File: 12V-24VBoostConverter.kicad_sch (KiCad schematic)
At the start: 16 parts, among them IC2 TPS613771RYHR

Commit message: small rev3 changes
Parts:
- added C22, C23: 22u, symbol Device:C
- C12: value 56u -> 22u
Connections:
- net GND: now also C22.2, C23.2
- net at C12.1, C41.1, F3.1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: now also C22.1, C23.1
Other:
- note removed: "change 56uF into 22u"
- moved on the sheet: C41

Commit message: revA4
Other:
- moved on the sheet: C10, C11, C12, C22, C23, C41, C7, C8, C9, F3, IC2, L2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

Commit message: RevA5
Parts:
- added D6: D_Schottky, SK34A-LTP, symbol Device:D_Schottky
- C10, C11, C9: footprint (none) -> Capacitor_SMD:C_0603_1608Metric
- C12, C22, C23, C41, C7, C8: footprint (none) -> Capacitor_SMD:C_0805_2012Metric
- F3: footprint (none) -> Fuse:Fuse_0805_2012Metric
- L2: footprint (none) -> Inductor_SMD:L_0603_1608Metric
- R10, R11, R12, R7: footprint (none) -> Resistor_SMD:R_0603_1608Metric
- R8: value 884.946 -> 1k; footprint (none) -> Resistor_SMD:R_0603_1608Metric
- R9: value 15k -> 29.4k; footprint (none) -> Resistor_SMD:R_0603_1608Metric
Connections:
- net at C12.1, C22.1, C23.1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: now also D6.2 (A); no longer F3.1
- new net: D6.1 (K), F3.1
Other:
- note added: "Ipeak = 0.54 * 160k/29.4k (standard component) Ipeak = 2.938 A"
- note added: "find new diode w low voltage drop"
- note removed: "Ipeak = I(avg input) + I(L)/2 = 5+ 0.75 = 5.75 --> 6A I(L) = 0.3 * 5 = 1.5 Ipeak = 6A 6 = 0.54 * 160k/Rlim Rlim = 14.4k or Ipeak = 0.54 * 160k/15k (standard component) Ipeak = 5.76A"
- moved on the sheet: F3
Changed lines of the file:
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@@
 		)
 	)
-	(text "Ipeak = I(avg input) + I(L)/2 = 5+ 0.75 = 5.75 --> 6A\nI(L) = 0.3 * 5 = 1.5\nIpeak = 6A\n6 = 0.54 * 160k/Rlim\nRlim = 14.4k\n\nor\n\nIpeak = 0.54 * 160k/15k (standard component)\nIpeak = 5.76A"
+	(text "Ipeak = 0.54 * 160k/29.4k (standard component)\nIpeak = 2.938 A"
 		(exclude_from_sim no)
-		(at 101.6 117.094 0)
+		(at 101.854 109.728 0)
 		(effects
 			(font
@@
 		)
 	)
+	(text "find new diode w low voltage drop"
+		(exclude_from_sim no)
+		(at 127.254 27.178 0)
+		(effects
+			(font
+				(size 1.27 1.27)
+			)
+			(justify left)
+		)
+	)
 	(junction
 		(at 86.36 29.21)
@@
 	(wire
 		(pts
+			(xy 128.27 43.18) (xy 132.08 43.18)
+		)
+		(stroke
+			(width 0)
+			(type default)
+		)
+	)
+	(wire
+		(pts
 			(xy 54.61 52.07) (xy 54.61 54.61)
 		)
@@
 	(wire
 		(pts
+			(xy 152.4 43.18) (xy 162.56 43.18)
+		)
+		(stroke
+			(width 0)
+			(type default)
+		)
+	)
+	(wire
+		(pts
 			(xy 128.27 49.53) (xy 128.27 52.07)
 		)
@@
 	(wire
 		(pts
-			(xy 149.86 43.18) (xy 162.56 43.18)
-		)
-		(stroke
-			(width 0)
-			(type default)
-		)
-	)
-	(wire
-		(pts
 			(xy 93.98 29.21) (xy 95.25 29.21)
 		)
@@
 	(wire
 		(pts
-			(xy 128.27 43.18) (xy 142.24 43.18)
-		)
-		(stroke
-			(width 0)
-			(type default)
-		)
-	)
-	(wire
-		(pts
 			(xy 138.43 59.69) (xy 138.43 62.23)
 		)
@@
 	(wire
 		(pts
+			(xy 139.7 43.18) (xy 144.78 43.18)
+		)
+		(stroke
+			(width 0)
+			(type default)
+		)
+	)
+	(wire
+		(pts
 			(xy 87.63 66.04) (xy 87.63 69.85)
 		)
@@
 		(dnp no)
 		(property "Reference" "C10"
-			(at 99.314 80.518 0)
+			(at 100.076 80.264 0)
 			(effects
 				(font
@@
 			)
 		)
-		(property "Footprint" ""
+		(property "Footprint" "Capacitor_SMD:C_0603_1608Metric"
 			(at 96.8248 78.74 0)
 			(effects
@@
 			)
 		)
-		(property "Footprint" ""
+		(property "Footprint" "Capacitor_SMD:C_0805_2012Metric"
 			(at 86.6648 69.85 0)
 			(effects
@@
 			)
 		)
-		(property "Footprint" ""
+		(property "Footprint" "Capacitor_SMD:C_0603_1608Metric"
 			(at 91.7448 69.85 0)
 			(effects
@@
 			)
 		)
-		(property "Value" "884.946"
+		(property "Value" "1k"
 			(at 55.88 49.784 0)
 			(effects
@@
 			)
 		)
-		(property "Footprint" ""
+		(property "Footprint" "Resistor_SMD:R_0603_1608Metric"
 			(at 52.832 48.26 90)
 			(effects
@@
 			)
 		)
-		(property "Footprint" ""
+		(property "Footprint" "Resistor_SMD:R_0603_1608Metric"
 			(at 52.832 38.1 90)
 			(effects
@@
 			)
 		)
-		(property "Footprint" ""
+		(property "Footprint" "Resistor_SMD:R_0603_1608Metric"
 			(at 117.602 50.8 90)
 			(effects
@@
 			)
 		)
-		(property "Footprint" ""
+		(property "Footprint" "Inductor_SMD:L_0603_1608Metric"
 			(at 90.17 29.21 0)
 			(effects
@@
 			)
 		)
-		(property "Footprint" ""
+		(property "Footprint" "Capacitor_SMD:C_0805_2012Metric"
 			(at 68.2752 38.1 0)
 			(effects
@@
 			)
 		)
-		(property "Footprint" ""
+		(property "Footprint" "Resistor_SMD:R_0603_1608Metric"
 			(at 117.602 67.31 90)
 			(effects
@@
 			)
 		)
-		(property "Footprint" ""
+		(property "Footprint" "Capacitor_SMD:C_0603_1608Metric"
 			(at 104.14 28.2448 0)
 			(effects
@@
 			)
 		)
-		(property "Footprint" ""
+		(property "Footprint" "Resistor_SMD:R_0603_1608Metric"
 			(at 96.012 73.66 90)
 			(effects
@@
 			)
 		)
-		(property "Value" "15k"
+		(property "Value" "29.4k"
 			(at 68.834 58.42 0)
 			(effects
@@
 			)
 		)
-		(property "Footprint" ""
+		(property "Footprint" "Resistor_SMD:R_0603_1608Metric"
 			(at 65.532 57.15 90)
 			(effects
@@
 	)
 	(symbol
+		(lib_id "Device:D_Schottky")
+		(at 135.89 43.18 0)
+		(mirror y)
+		(unit 1)
+		(exclude_from_sim no)
+		(in_bom yes)
+		(on_board yes)
+		(dnp no)
+		(property "Reference" "D6"
+			(at 136.2075 36.83 0)
+			(effects
+				(font
+					(size 1.27 1.27)
+				)
+			)
+		)
+		(property "Value" "D_Schottky"
+			(at 136.2075 39.37 0)
+			(effects
+				(font
+					(size 1.27 1.27)
+				)
+			)
+		)
+		(property "Footprint" "SK34A-LTP"
+			(at 135.89 43.18 0)
+			(effects
+				(font
+					(size 1.27 1.27)
+				)
+				(hide yes)
+			)
+		)
+		(property "Datasheet" "https://www.mouser.com/datasheet/3/225/1/SK32A-L-SK310A-L(SMA).pdf"
+			(at 135.89 43.18 0)
+			(effects
+				(font
+					(size 1.27 1.27)
+				)
+				(hide yes)
+			)
+		)
+		(property "Description" "Schottky diode"
+			(at 135.89 43.18 0)
+			(effects
+				(font
+					(size 1.27 1.27)
+				)
+				(hide yes)
+			)
+		)
+		(pin "1"
+		)
+		(pin "2"
+		)
+		(instances
+			(project ""
+				(path "/d45494af-ff47-4110-bed2-dd613b557244/a5946dd4-2cac-491d-9b85-f213ab9011e7"
+					(reference "D6")
+					(unit 1)
+				)
+			)
+		)
+	)
+	(symbol
 		(lib_id "Device:C")
 		(at 138.43 55.88 0)
@@
 			)
 		)
-		(property "Footprint" ""
+		(property "Footprint" "Capacitor_SMD:C_0805_2012Metric"
 			(at 139.3952 59.69 0)
 			(effects
@@
 	(symbol
 		(lib_id "Device:Fuse")
-		(at 146.05 43.18 90)
+		(at 148.59 43.18 90)
 		(unit 1)
 		(exclude_from_sim no)
@@
 		(dnp no)
 		(property "Reference" "F3"
-			(at 147.066 41.148 90)
+			(at 149.606 41.148 90)
 			(effects
 				(font
@@
 		)
 		(property "Value" "5"
-			(at 146.558 45.466 90)
+			(at 149.098 45.466 90)
 			(effects
 				(font
@@
 			)
 		)
-		(property "Footprint" ""
-			(at 146.05 44.958 90)
+		(property "Footprint" "Fuse:Fuse_0805_2012Metric"
+			(at 148.59 44.958 90)
 			(effects
 				(font
@@
 		)
 		(property "Datasheet" "~"
-			(at 146.05 43.18 0)
+			(at 148.59 43.18 0)
 			(effects
 				(font
@@
 		)
 		(property "Description" "Fuse"
-			(at 146.05 43.18 0)
+			(at 148.59 43.18 0)
 			(effects
 				(font
@@
 			)
 		)
-		(property "Footprint" ""
+		(property "Footprint" "Capacitor_SMD:C_0805_2012Metric"
 			(at 129.2352 59.69 0)
 			(effects
@@
 			)
 		)
-		(property "Footprint" ""
+		(property "Footprint" "Capacitor_SMD:C_0805_2012Metric"
 			(at 149.5552 59.69 0)
 			(effects
@@
 			)
 		)
-		(property "Footprint" ""
+		(property "Footprint" "Capacitor_SMD:C_0805_2012Metric"
 			(at 159.7152 59.69 0)
 			(effects

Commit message: RevA5 small changes
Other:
- note removed: "find new diode w low voltage drop"
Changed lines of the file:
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@@
-		)
-	)
-	(text "find new diode w low voltage drop"
-		(exclude_from_sim no)
-		(at 127.254 27.178 0)
-		(effects
-			(font
-				(size 1.27 1.27)
-			)
-			(justify left)
 		)
 	)

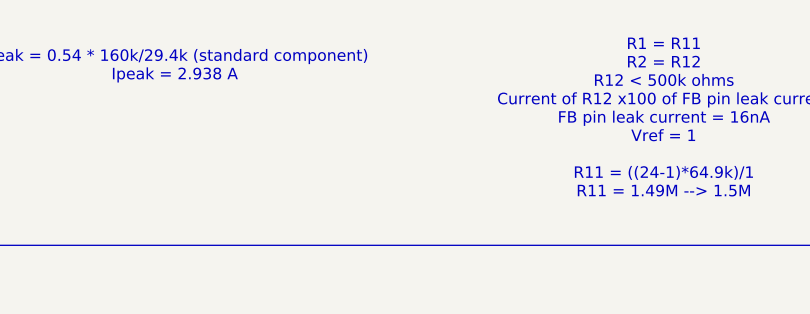
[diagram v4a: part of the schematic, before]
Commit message: RevA6 footprint updates
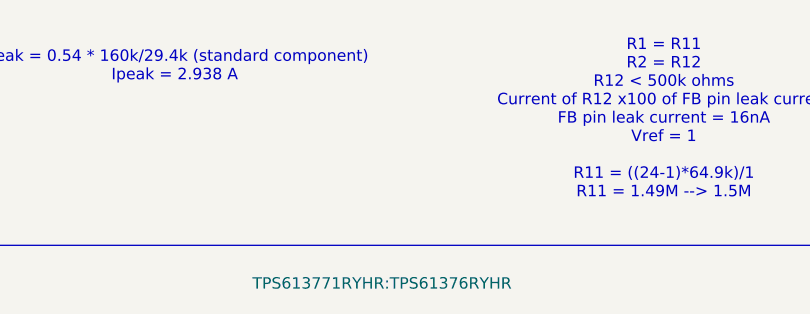
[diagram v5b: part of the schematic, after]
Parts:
- D6: footprint SK34A-LTP -> SK32A_LTP:SDO_DO-214AC-SMA_MCE
- IC2: footprint TPS61376RYHR -> TPS613771RYHR:TPS61376RYHR
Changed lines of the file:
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@@
 			)
 		)
-		(property "Footprint" "TPS61376RYHR"
+		(property "Footprint" "TPS613771RYHR:TPS61376RYHR"
 			(at 110.49 133.02 0)
 			(effects
@@
 				)
 				(justify left top)
-				(hide yes)
 			)
 		)
@@
 			)
 		)
-		(property "Footprint" "SK34A-LTP"
+		(property "Footprint" "SK32A_LTP:SDO_DO-214AC-SMA_MCE"
 			(at 135.89 43.18 0)
 			(effects

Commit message: RevA7 layout
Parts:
- IC2: footprint TPS613771RYHR:TPS61376RYHR -> TPS613771RYHR:VQFN-HR13_RYH_TEX
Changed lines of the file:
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@@
 			)
 		)
-		(property "Footprint" "TPS613771RYHR:TPS61376RYHR"
+		(property "Footprint" "TPS613771RYHR:VQFN-HR13_RYH_TEX"
 			(at 110.49 133.02 0)
 			(effects

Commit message: RevA9 for review
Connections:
- net 24VOut_B4Diodes: now reaches C12.1, C22.1, C23.1, C41.1, D6.2 (A), IC2.4 (VSENSE_1), IC2.5 (VOUT), R11.1

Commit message: RevA9 small changes
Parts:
- renumbered C7 to C1, C8 to C2, C9 to C3, C10 to C4, C11 to C5, C12 to C6, C41 to C7, C22 to C8, C23 to C9, D6 to D1, F3 to F1, IC2 to IC1, L2 to L1, R11 to R10, R12 to R11, R7 to R6, R8 to R7, R9 to R8, R10 to R9
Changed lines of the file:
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@@
 		(on_board yes)
 		(dnp no)
-		(property "Reference" "C10"
+		(property "Reference" "C4"
 			(at 100.076 80.264 0)
 			(effects
@@
 			(project "PS-ChargerInterfacePCB"
 				(path "/d45494af-ff47-4110-bed2-dd613b557244/a5946dd4-2cac-491d-9b85-f213ab9011e7"
-					(reference "C10")
+					(reference "C4")
 					(unit 1)
 				)
@@
 		(dnp no)
 		(fields_autoplaced yes)
-		(property "Reference" "#PWR038"
+		(property "Reference" "#PWR022"
 			(at 68.58 54.61 0)
 			(effects
@@
 			(project "PS-ChargerInterfacePCB"
 				(path "/d45494af-ff47-4110-bed2-dd613b557244/a5946dd4-2cac-491d-9b85-f213ab9011e7"
-					(reference "#PWR038")
+					(reference "#PWR022")
 					(unit 1)
 				)
@@
 		(on_board yes)
 		(dnp no)
-		(property "Reference" "C8"
+		(property "Reference" "C2"
 			(at 85.598 71.374 0)
 			(effects
@@
 			(project "PS-ChargerInterfacePCB"
 				(path "/d45494af-ff47-4110-bed2-dd613b557244/a5946dd4-2cac-491d-9b85-f213ab9011e7"
-					(reference "C8")
+					(reference "C2")
 					(unit 1)
 				)
@@
 		(on_board yes)
 		(dnp no)
-		(property "Reference" "C9"
+		(property "Reference" "C3"
 			(at 94.234 71.374 0)
 			(effects
@@
 			(project "PS-ChargerInterfacePCB"
 				(path "/d45494af-ff47-4110-bed2-dd613b557244/a5946dd4-2cac-491d-9b85-f213ab9011e7"
-					(reference "C9")
+					(reference "C3")
 					(unit 1)
 				)
@@
 		(dnp no)
 		(fields_autoplaced yes)
-		(property "Reference" "#PWR010"
+		(property "Reference" "#PWR020"
 			(at 67.31 45.72 0)
 			(effects
@@
 			(project "PS-ChargerInterfacePCB"
 				(path "/d45494af-ff47-4110-bed2-dd613b557244/a5946dd4-2cac-491d-9b85-f213ab9011e7"
-					(reference "#PWR010")
+					(reference "#PWR020")
 					(unit 1)
 				)
@@
 		(on_board yes)
 		(dnp no)
-		(property "Reference" "R8"
+		(property "Reference" "R7"
 			(at 55.88 47.244 0)
 			(effects
@@
 			(project "PS-ChargerInterfacePCB"
 				(path "/d45494af-ff47-4110-bed2-dd613b557244/a5946dd4-2cac-491d-9b85-f213ab9011e7"
-					(reference "R8")
+					(reference "R7")
 					(unit 1)
 				)
@@
 		(on_board yes)
 		(dnp no)
-		(property "Reference" "R7"
+		(property "Reference" "R6"
 			(at 56.134 36.576 0)
 			(effects
@@
 			(project "PS-ChargerInterfacePCB"
 				(path "/d45494af-ff47-4110-bed2-dd613b557244/a5946dd4-2cac-491d-9b85-f213ab9011e7"
-					(reference "R7")
+					(reference "R6")
 					(unit 1)
 				)
@@
 		(on_board yes)
 		(dnp no)
-		(property "Reference" "#PWR012"
+		(property "Reference" "#PWR023"
 			(at 100.33 73.66 0)
 			(effects
@@
 			(project "PS-ChargerInterfacePCB"
 				(path "/d45494af-ff47-4110-bed2-dd613b557244/a5946dd4-2cac-491d-9b85-f213ab9011e7"
-					(reference "#PWR012")
+					(reference "#PWR023")
 					(unit 1)
 				)
@@
 		(on_board yes)
 		(dnp no)
-		(property "Reference" "R11"
+		(property "Reference" "R10"
 			(at 120.904 49.53 0)
 			(effects
@@
 			(project "PS-ChargerInterfacePCB"
 				(path "/d45494af-ff47-4110-bed2-dd613b557244/a5946dd4-2cac-491d-9b85-f213ab9011e7"
-					(reference "R11")
+					(reference "R10")
 					(unit 1)
 				)
@@
 		(on_board yes)
 		(dnp no)
-		(property "Reference" "L2"
+		(property "Reference" "L1"
 			(at 90.17 27.432 90)
 			(effects
@@
 			(project "PS-ChargerInterfacePCB"
 				(path "/d45494af-ff47-4110-bed2-dd613b557244/a5946dd4-2cac-491d-9b85-f213ab9011e7"
-					(reference "L2")
+					(reference "L1")
 					(unit 1)
 				)
@@
 		(on_board yes)
 		(dnp no)
-		(property "Reference" "C7"
+		(property "Reference" "C1"
 			(at 67.564 32.258 0)
 			(effects
@@
 			(project "PS-ChargerInterfacePCB"
 				(path "/d45494af-ff47-4110-bed2-dd613b557244/a5946dd4-2cac-491d-9b85-f213ab9011e7"
-					(reference "C7")
+					(reference "C1")
 					(unit 1)
 				)
@@
 		(on_board yes)
 		(dnp no)
-		(property "Reference" "IC2"
+		(property "Reference" "IC1"
 			(at 118.11 36.7598 0)
 			(effects
@@
 			(project "PS-ChargerInterfacePCB"
 				(path "/d45494af-ff47-4110-bed2-dd613b557244/a5946dd4-2cac-491d-9b85-f213ab9011e7"
-					(reference "IC2")
+					(reference "IC1")
 					(unit 1)
 				)
@@
 		(on_board yes)
 		(dnp no)
-		(property "Reference" "R12"
+		(property "Reference" "R11"
 			(at 120.65 66.04 0)
 			(effects
@@
 			(project "PS-ChargerInterfacePCB"
 				(path "/d45494af-ff47-4110-bed2-dd613b557244/a5946dd4-2cac-491d-9b85-f213ab9011e7"
-					(reference "R12")
+					(reference "R11")
 					(unit 1)
 				)
@@
 		(dnp no)
 		(fields_autoplaced yes)
-		(property "Reference" "#PWR011"
+		(property "Reference" "#PWR021"
 			(at 67.31 68.58 0)
 			(effects
@@
 			(project "PS-ChargerInterfacePCB"
 				(path "/d45494af-ff47-4110-bed2-dd613b557244/a5946dd4-2cac-491d-9b85-f213ab9011e7"
-					(reference "#PWR011")
+					(reference "#PWR021")
 					(unit 1)
 				)
@@
 		(on_board yes)
 		(dnp no)
-		(property "Reference" "C11"
+		(property "Reference" "C5"
 			(at 97.536 28.194 90)
 			(effects
@@
 			(project "PS-ChargerInterfacePCB"
 				(path "/d45494af-ff47-4110-bed2-dd613b557244/a5946dd4-2cac-491d-9b85-f213ab9011e7"
-					(reference "C11")
+					(reference "C5")
 					(unit 1)
 				)
@@
 		(on_board yes)
 		(dnp no)
-		(property "Reference" "R10"
+		(property "Reference" "R9"
 			(at 99.568 72.39 0)
 			(effects
@@
 			(project "PS-ChargerInterfacePCB"
 				(path "/d45494af-ff47-4110-bed2-dd613b557244/a5946dd4-2cac-491d-9b85-f213ab9011e7"
-					(reference "R10")
+					(reference "R9")
 					(unit 1)
 				)
@@
 		(on_board yes)
 		(dnp no)
-		(property "Reference" "R9"
+		(property "Reference" "R8"
 			(at 68.834 55.88 0)
 			(effects
@@
 			(project "PS-ChargerInterfacePCB"
 				(path "/d45494af-ff47-4110-bed2-dd613b557244/a5946dd4-2cac-491d-9b85-f213ab9011e7"
-					(reference "R9")
+					(reference "R8")
 					(unit 1)
 				)
@@
 		(on_board yes)
 		(dnp no)
-		(property "Reference" "D6"
+		(property "Reference" "D1"
 			(at 136.2075 36.83 0)
 			(effects
@@
 			(project ""
 				(path "/d45494af-ff47-4110-bed2-dd613b557244/a5946dd4-2cac-491d-9b85-f213ab9011e7"
-					(reference "D6")
+					(reference "D1")
 					(unit 1)
 				)
@@
 		(on_board yes)
 		(dnp no)
-		(property "Reference" "C41"
+		(property "Reference" "C7"
 			(at 140.97 54.61 0)
 			(effects
@@
 			(project "PS-ChargerInterfacePCB"
 				(path "/d45494af-ff47-4110-bed2-dd613b557244/a5946dd4-2cac-491d-9b85-f213ab9011e7"
-					(reference "C41")
+					(reference "C7")
 					(unit 1)
 				)
@@
 		(on_board yes)
 		(dnp no)
-		(property "Reference" "F3"
+		(property "Reference" "F1"
 			(at 149.606 41.148 90)
 			(effects
@@
 			(project "PS-ChargerInterfacePCB"
 				(path "/d45494af-ff47-4110-bed2-dd613b557244/a5946dd4-2cac-491d-9b85-f213ab9011e7"
-					(reference "F3")
+					(reference "F1")
 					(unit 1)
 				)
@@
 		(dnp no)
 		(fields_autoplaced yes)
-		(property "Reference" "#PWR013"
+		(property "Reference" "#PWR024"
 			(at 104.14 95.25 0)
 			(effects
@@
 			(project "PS-ChargerInterfacePCB"
 				(path "/d45494af-ff47-4110-bed2-dd613b557244/a5946dd4-2cac-491d-9b85-f213ab9011e7"
-					(reference "#PWR013")
+					(reference "#PWR024")
 					(unit 1)
 				)
@@
 		(on_board yes)
 		(dnp no)
-		(property "Reference" "C12"
+		(property "Reference" "C6"
 			(at 130.81 54.61 0)
 			(effects
@@
 			(project "PS-ChargerInterfacePCB"
 				(path "/d45494af-ff47-4110-bed2-dd613b557244/a5946dd4-2cac-491d-9b85-f213ab9011e7"
-					(reference "C12")
+					(reference "C6")
 					(unit 1)
 				)
@@
 		(on_board yes)
 		(dnp no)
-		(property "Reference" "C22"
+		(property "Reference" "C8"
 			(at 151.13 54.61 0)
 			(effects
@@
 			(project "PS-ChargerInterfacePCB"
 				(path "/d45494af-ff47-4110-bed2-dd613b557244/a5946dd4-2cac-491d-9b85-f213ab9011e7"
-					(reference "C22")
+					(reference "C8")
 					(unit 1)
 				)
@@
 		(dnp no)
 		(fields_autoplaced yes)
-		(property "Reference" "#PWR014"
+		(property "Reference" "#PWR025"
 			(at 134.62 69.85 0)
 			(effects
@@
 			(project "PS-ChargerInterfacePCB"
 				(path "/d45494af-ff47-4110-bed2-dd613b557244/a5946dd4-2cac-491d-9b85-f213ab9011e7"
-					(reference "#PWR014")
+					(reference "#PWR025")
 					(unit 1)
 				)
@@
 		(dnp no)
 		(fields_autoplaced yes)
-		(property "Reference" "#PWR09"
+		(property "Reference" "#PWR019"
 			(at 54.61 60.96 0)
 			(effects
@@
 			(project "PS-ChargerInterfacePCB"
 				(path "/d45494af-ff47-4110-bed2-dd613b557244/a5946dd4-2cac-491d-9b85-f213ab9011e7"
-					(reference "#PWR09")
+					(reference "#PWR019")
 					(unit 1)
 				)
@@
 		(on_board yes)
 		(dnp no)
-		(property "Reference" "C23"
+		(property "Reference" "C9"
 			(at 161.29 54.61 0)
 			(effects
@@
 			(project "PS-ChargerInterfacePCB"
 				(path "/d45494af-ff47-4110-bed2-dd613b557244/a5946dd4-2cac-491d-9b85-f213ab9011e7"
-					(reference "C23")
-					(unit 1)
-				)
+					(reference "C9")
+					(unit 1)
+				)
